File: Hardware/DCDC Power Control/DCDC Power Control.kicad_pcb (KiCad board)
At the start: 2 copper layers, 49 x 48 mm, 33 parts, among them J1 Conn_01x03, J2 Conn_01x02, J3 Conn_01x02, J4 Screw_Terminal_01x02, J5 Conn_01x01, Q2 SQJ479EP-T1_GE3, U1 CPC2025N

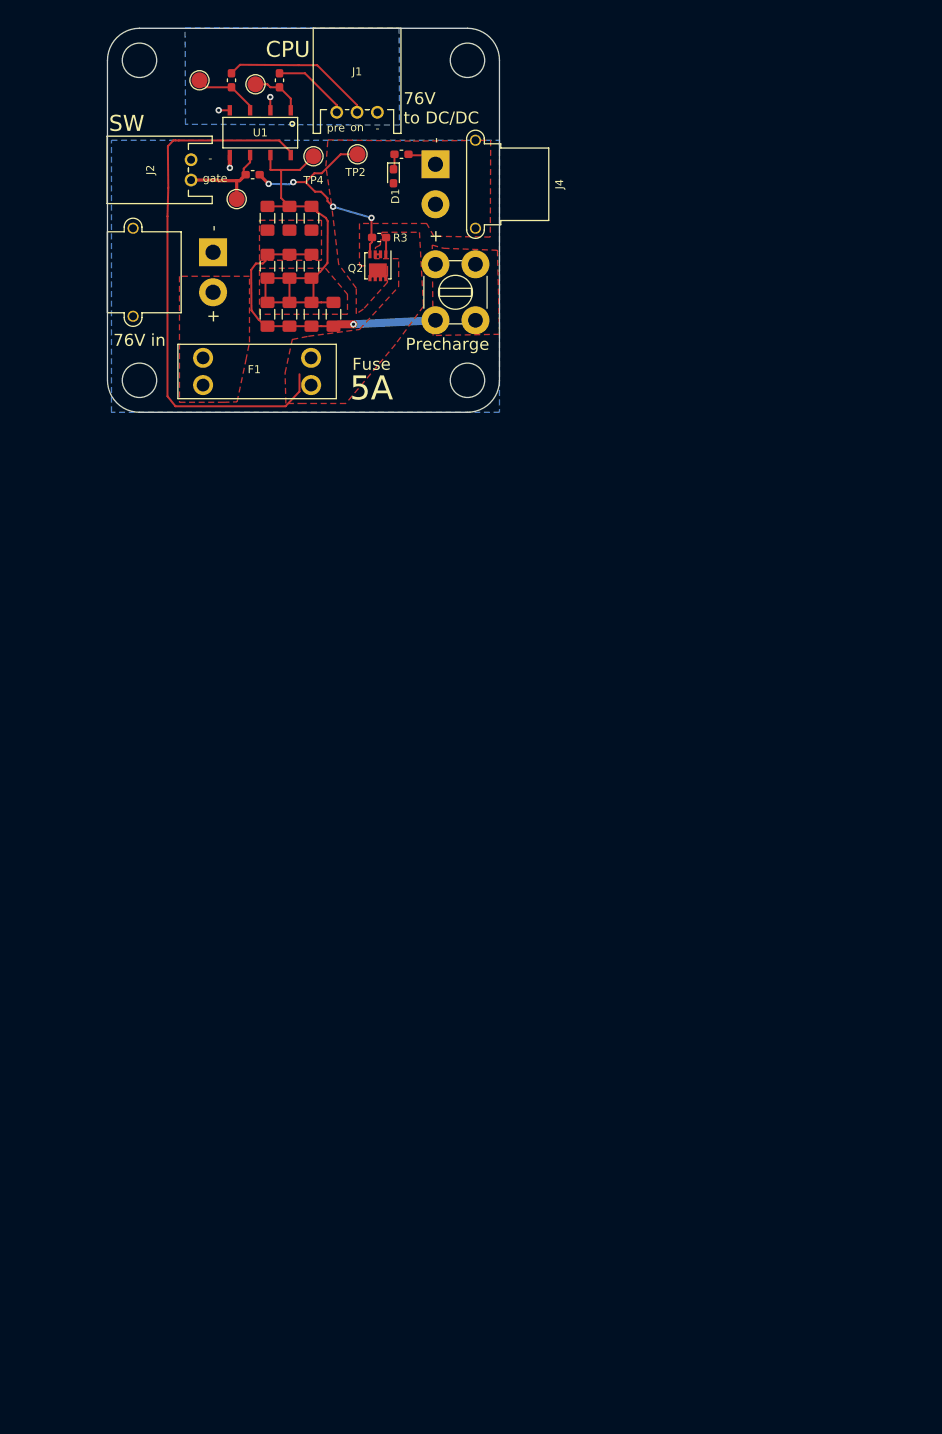
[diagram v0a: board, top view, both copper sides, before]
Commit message: Revision 2 of the DCDC Control PCB.
Now with precharge for both DC/DC and VESC, 150 ohm 45 W precharge resistors
(up to three per device).

Microcontroller to control the sequencing. ADC measurement of in vs out voltage
to determine when precharge is complete.
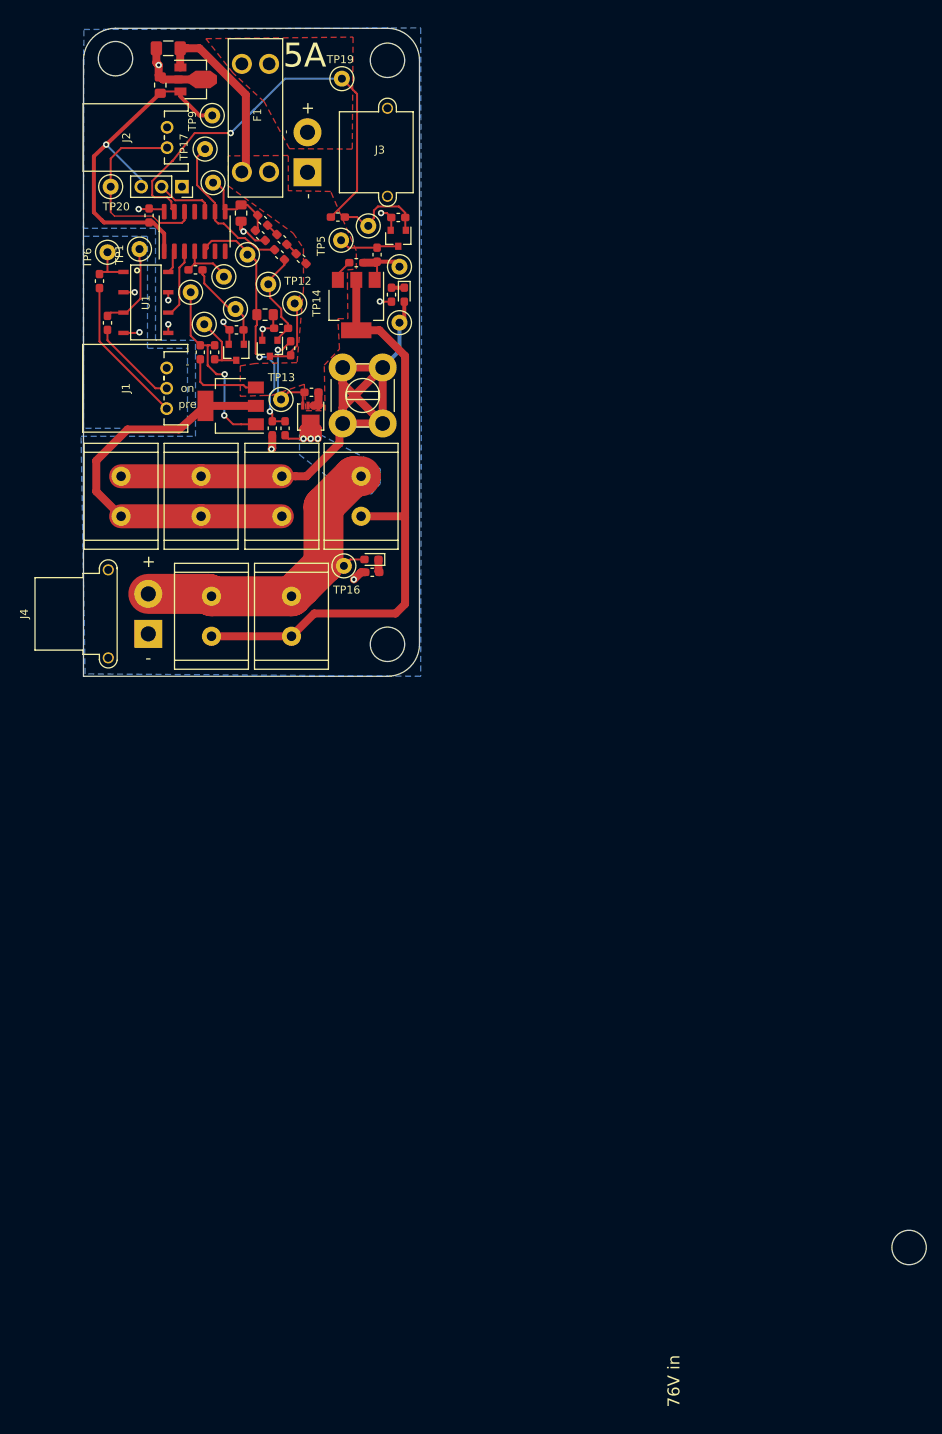
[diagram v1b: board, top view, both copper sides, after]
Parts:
- removed the H1 at (105.0, 46.0)
- removed H2: MountingHole, MountingHole:MountingHole_4.3mm_M4_ISO14580
- added C1: 100 nF/3.3V, Capacitor_SMD:C_0805_2012Metric_Pad1.15x1.40mm_HandSolder, F.Cu at (117.7, 65.1)
- added C2: 1 uF / 80V, Capacitor_SMD:C_1206_3216Metric_Pad1.42x1.75mm_HandSolder, F.Cu at (108.6, 44.5)
- added C3: 22 uF/3.3V, Capacitor_SMD:C_0805_2012Metric_Pad1.15x1.40mm_HandSolder, F.Cu at (107.6, 49.1)
- added C4: 100 nF/3.3V, Capacitor_SMD:C_0805_2012Metric_Pad1.15x1.40mm_HandSolder, F.Cu at (120.7, 77.8)
- added C5: 100 nF/3.3V, Capacitor_SMD:C_0603_1608Metric_Pad1.05x0.95mm_HandSolder, F.Cu at (106.2, 65.4)
- added D2: LED, LED_SMD:LED_0603_1608Metric_Pad1.05x0.95mm_HandSolder, F.Cu at (134.0, 108.4)
- added H1: MountingHole, MountingHole:MountingHole_4.3mm_M4_ISO14580, F.Cu at (102.0, 46.0)
- added H1: MountingHole, MountingHole:MountingHole_4.3mm_M4_ISO14580, F.Cu at (136.0, 46.0)
- added J6: Conn_01x03_Female, Connector_PinSocket_2.54mm:PinSocket_1x03_P2.54mm_Vertical, F.Cu at (110.3, 61.8)
- added Q1: BSS123, Package_TO_SOT_SMD:SOT-23, F.Cu at (117.1, 82.5)
- added Q3: BSS123, Package_TO_SOT_SMD:SOT-23, F.Cu at (137.3, 68.2)
- added Q4: MCT06P10, Package_TO_SOT_SMD:SOT-223-3_TabPin2, F.Cu at (132.1, 76.6)
- added Q5: BSS123, Package_TO_SOT_SMD:SOT-23, F.Cu at (121.3, 82.0)
- added Q6: SQJ479EP-T1_GE3, Package_SO:Vishay_PowerPAK_1212-8_Single, F.Cu at (126.4, 90.6)
- added R16: 15K, Resistor_SMD:R_0603_1608Metric_Pad1.05x0.95mm_HandSolder, F.Cu at (132.1, 71.3)
- added R17: 56k, Resistor_SMD:R_0603_1608Metric_Pad1.05x0.95mm_HandSolder, F.Cu at (134.7, 70.3)
- added R18: 150 Ohm, 45W, Resistor_THT:R_Radial_Power_L13.0mm_W9.0mm_P5.00mm, F.Cu at (124.0, 113.0)
- added R19: 10k, Resistor_SMD:R_0603_1608Metric_Pad1.05x0.95mm_HandSolder, F.Cu at (122.7, 79.5)
- added R20: 15K, Resistor_SMD:R_0603_1608Metric_Pad1.05x0.95mm_HandSolder, F.Cu at (126.5, 87.5)
- added R21: 56k, Resistor_SMD:R_0603_1608Metric_Pad1.05x0.95mm_HandSolder, F.Cu at (123.9, 82.0)
- added R22: 1k, Resistor_SMD:R_0603_1608Metric_Pad1.05x0.95mm_HandSolder, F.Cu at (112.0, 72.2)
- added R23: 1k, Resistor_SMD:R_0603_1608Metric_Pad1.05x0.95mm_HandSolder, F.Cu at (129.8, 65.6)
- added R24: 1k, Resistor_SMD:R_0603_1608Metric_Pad1.05x0.95mm_HandSolder, F.Cu at (122.5, 70.3)
- added R25: 150 Ohm, 45W, Resistor_THT:R_Radial_Power_L13.0mm_W9.0mm_P5.00mm, F.Cu at (102.7, 98.0)
- added R26: 150 Ohm, 45W, Resistor_THT:R_Radial_Power_L13.0mm_W9.0mm_P5.00mm, F.Cu at (122.8, 98.0)
- added R27: 150 Ohm, 45W, Resistor_THT:R_Radial_Power_L13.0mm_W9.0mm_P5.00mm, F.Cu at (132.7, 98.0)
- added R28: 150 Ohm, 45W, Resistor_THT:R_Radial_Power_L13.0mm_W9.0mm_P5.00mm, F.Cu at (114.0, 113.0)
- added TP10: TestPoint, TestPoint:TestPoint_Loop_D2.50mm_Drill1.0mm_LowProfile, F.Cu at (117.0, 77.1)
- added TP11: TestPoint, TestPoint:TestPoint_Loop_D2.50mm_Drill1.0mm_LowProfile, F.Cu at (133.6, 66.7)
- added TP12: TestPoint, TestPoint:TestPoint_Loop_D2.50mm_Drill1.0mm_LowProfile, F.Cu at (121.1, 74.0)
- added TP13: TestPoint, TestPoint:TestPoint_Loop_D2.50mm_Drill1.0mm_LowProfile, F.Cu at (122.7, 88.4)
- added TP14: TestPoint, TestPoint:TestPoint_Loop_D2.50mm_Drill1.0mm_LowProfile, F.Cu at (124.4, 76.4)
- added TP15: TestPoint, TestPoint:TestPoint_Loop_D2.50mm_Drill1.0mm_LowProfile, F.Cu at (137.5, 78.8)
- added TP16: TestPoint, TestPoint:TestPoint_Loop_D2.50mm_Drill1.0mm_LowProfile, F.Cu at (130.6, 109.2)
- added TP17: TestPoint, TestPoint:TestPoint_Loop_D2.50mm_Drill1.0mm_LowProfile, F.Cu at (113.2, 57.1)
- added TP18: TestPoint, TestPoint:TestPoint_Loop_D2.50mm_Drill1.0mm_LowProfile, F.Cu at (115.5, 73.0)
- added TP19: TestPoint, TestPoint:TestPoint_Loop_D2.50mm_Drill1.0mm_LowProfile, F.Cu at (130.3, 48.3)
- added TP20: TestPoint, TestPoint:TestPoint_Loop_D2.50mm_Drill1.0mm_LowProfile, F.Cu at (101.4, 61.8)
- added TP5: TestPoint, TestPoint:TestPoint_Loop_D2.50mm_Drill1.0mm_LowProfile, F.Cu at (130.2, 68.5)
- added TP7: TestPoint, TestPoint:TestPoint_Loop_D2.50mm_Drill1.0mm_LowProfile, F.Cu at (114.2, 61.3)
- added TP8: TestPoint, TestPoint:TestPoint_Loop_D2.50mm_Drill1.0mm_LowProfile, F.Cu at (118.5, 70.3)
- added TP9: TestPoint, TestPoint:TestPoint_Loop_D2.50mm_Drill1.0mm_LowProfile, F.Cu at (114.1, 52.9)
- added U2: NCP785AH33T1G, Package_TO_SOT_SMD:SOT-89-3, F.Cu at (111.6, 48.4)
- added U3: ATtiny414-SS, Package_SO:SOIC-14_3.9x8.7mm_P1.27mm, F.Cu at (111.9, 67.4)
- D1: value LED -> Or LED
- Q2: value SQJ479EP-T1_GE3 -> MCT06P10; footprint Package_SO:Vishay_PowerPAK_1212-8_Single -> Package_TO_SOT_SMD:SOT-223-3_TabPin2
- R10: value 11k/500mW -> 13.3k; footprint Resistor_SMD:R_1206_3216Metric_Pad1.42x1.75mm_HandSolder -> Resistor_SMD:R_0603_1608Metric_Pad1.05x0.95mm_HandSolder
- R11: value 11k/500mW -> 100k; footprint Resistor_SMD:R_1206_3216Metric_Pad1.42x1.75mm_HandSolder -> Resistor_SMD:R_0603_1608Metric_Pad1.05x0.95mm_HandSolder
- R12: value 11k/500mW -> 15K; footprint Resistor_SMD:R_1206_3216Metric_Pad1.42x1.75mm_HandSolder -> Resistor_SMD:R_0603_1608Metric_Pad1.05x0.95mm_HandSolder
- R13: value 11k/500mW -> 56k; footprint Resistor_SMD:R_1206_3216Metric_Pad1.42x1.75mm_HandSolder -> Resistor_SMD:R_0603_1608Metric_Pad1.05x0.95mm_HandSolder
- R14: value 11k/500mW -> 150 Ohm, 45W; footprint Resistor_SMD:R_1206_3216Metric_Pad1.42x1.75mm_HandSolder -> Resistor_THT:R_Radial_Power_L13.0mm_W9.0mm_P5.00mm
- R15: value 11k/500mW -> 10k; footprint Resistor_SMD:R_1206_3216Metric_Pad1.42x1.75mm_HandSolder -> Resistor_SMD:R_0603_1608Metric_Pad1.05x0.95mm_HandSolder
- R3: value 15K -> 47k 120 mW
- R4: value 56k -> 47k
- R5: value 10k -> 10M
- R6, R7: value 11k/500mW -> 10M; footprint Resistor_SMD:R_1206_3216Metric_Pad1.42x1.75mm_HandSolder -> Resistor_SMD:R_0603_1608Metric_Pad1.05x0.95mm_HandSolder
- R8: value 11k/500mW -> 1.33M; footprint Resistor_SMD:R_1206_3216Metric_Pad1.42x1.75mm_HandSolder -> Resistor_SMD:R_0603_1608Metric_Pad1.05x0.95mm_HandSolder
- R9: value 11k/500mW -> 300k; footprint Resistor_SMD:R_1206_3216Metric_Pad1.42x1.75mm_HandSolder -> Resistor_SMD:R_0603_1608Metric_Pad1.05x0.95mm_HandSolder
- TP1, TP2, TP3, TP4, TP6: footprint TestPoint:TestPoint_Pad_D2.0mm -> TestPoint:TestPoint_Loop_D2.50mm_Drill1.0mm_LowProfile
- moved H3 144.9 mm to (201.2, 194.4), turned to 90 degrees
- moved H4 73.7 mm to (136.0, 119.0), turned to 270 degrees
- moved J4 68.8 mm to (106.1, 117.7), turned to 90 degrees
- moved R4 51.9 mm to (134.1, 110.0)
- moved J1 41.9 mm to (108.4, 87.0), turned to 270 degrees
- moved R14 35.1 mm to (112.7, 98.0), turned to 270 degrees
- moved R1 34.1 mm to (101.0, 78.8), turned to 270 degrees
- moved R2 33.7 mm to (100.0, 73.6), turned to 270 degrees
- moved F1 31.7 mm to (119.5, 53.2), turned to 90 degrees
- moved TP6 28.0 mm to (101.0, 70.0), turned to 270 degrees
- moved TP2 27.1 mm to (111.4, 75.0), turned to 270 degrees
- moved U1 25.6 mm to (105.8, 76.3), turned to 270 degrees
- moved Q2 25.4 mm to (116.4, 89.2), turned to 180 degrees
- moved TP1 22.4 mm to (105.0, 69.6), turned to 270 degrees
- moved R9 20.3 mm to (123.2, 92.0), turned to 90 degrees
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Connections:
- net /ON renamed /DCDC_ON_IN
- net /PRECHARGE_ON renamed /VESC_PRECHARGE_IN
- D1 pad 2: Net-(D1-Pad2) -> /VESC_OUT
- J2 pad 2: /POWER_GATE -> /SWITCH_B
- J4 pad 2: Net-(D1-Pad2) -> /DCDC_OUT
- J5 pad 1: /PRECHARGE_POST_R -> /VESC_OUT
- Q2 pad 1: +BATT -> /Power Switches/Q2_GATE
- Q2 pad 2: +BATT -> /Power Switches/VESC_PRE_PRECHARGE
- R10 pad 1: /PRECHARGE_POST_R -> /Microcontroller/DCDC_ADC
- R10 pad 2: /PRECHARGE_PRE_R -> GNDPWR
- R11 pad 1: /PRECHARGE_POST_R -> Net-(Q1-Pad1)
- R11 pad 2: /PRECHARGE_PRE_R -> GNDPWR
- R12 pad 1: /PRECHARGE_POST_R -> +BATT
- R12 pad 2: /PRECHARGE_PRE_R -> /Power Switches/Q2_GATE
- R13 pad 1: /PRECHARGE_POST_R -> /Power Switches/Q2_GATE
- R13 pad 2: /PRECHARGE_PRE_R -> Net-(Q1-Pad3)
- R14 pad 1: /PRECHARGE_POST_R -> /VESC_OUT
- R14 pad 2: /PRECHARGE_PRE_R -> /Power Switches/VESC_PRE_PRECHARGE
- R15 pad 1: /PRECHARGE_POST_R -> Net-(Q3-Pad1)
- R15 pad 2: /PRECHARGE_PRE_R -> GNDPWR
- R3 pad 1: +BATT -> Net-(D1-Pad1)
- R3 pad 2: /Q2_GATE -> GNDPWR
- R4 pad 1: /Q2_GATE -> Net-(D2-Pad1)
- R4 pad 2: /POWER_GATE -> GNDPWR
- R5 pad 1: Net-(D1-Pad1) -> +BATT
- R5 pad 2: GNDPWR -> Net-(R5-Pad2)
- R6 pad 1: /PRECHARGE_POST_R -> Net-(R5-Pad2)
- R6 pad 2: /PRECHARGE_PRE_R -> Net-(R6-Pad2)
- R7 pad 1: /PRECHARGE_POST_R -> Net-(R6-Pad2)
- R7 pad 2: /PRECHARGE_PRE_R -> /Microcontroller/VBATT_ADC
- R8 pad 1: /PRECHARGE_POST_R -> /Microcontroller/VBATT_ADC
- R8 pad 2: /PRECHARGE_PRE_R -> GNDPWR
- R9 pad 1: /PRECHARGE_POST_R -> /DCDC_OUT
- R9 pad 2: /PRECHARGE_PRE_R -> /Microcontroller/DCDC_ADC
- TP2 pad 1: /Q2_GATE -> /Power Switches/Q2_GATE
- TP3 pad 1: /POWER_GATE -> Net-(Q1-Pad3)
- TP4 pad 1: /PRECHARGE_PRE_R -> /Power Switches/Q4_GATE
- U1 pad 6: /POWER_GATE -> /DCDC_ON
- U1 pad 7: /PRECHARGE_PRE_R -> GNDPWR
- U1 pad 8: +BATT -> /VESC_PRECHARGE
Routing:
- net /VESC_OUT: track 0.00 -> 83.0 mm
- net /Power Switches/DCDC_PRE_PRECHARGE: track 0.00 -> 76.2 mm
- net /Microcontroller/DCDC_PRECHARGE_GATE: track 0.00 -> 55.6 mm, vias 0 -> 1
- net /PRECHARGE_PRE_R: track 53.7 -> 0.00 mm
- net /DCDC_OUT: track 0.00 -> 52.4 mm, vias 0 -> 3
- net /Power Switches/VESC_PRE_PRECHARGE: track 0.00 -> 51.0 mm
- net +3V3: track 0.00 -> 45.9 mm, vias 0 -> 1
- net /PRECHARGE_POST_R: track 38.2 -> 0.00 mm, vias 1 -> 0
- net /Microcontroller/DCDC_ADC: track 0.00 -> 33.3 mm, vias 0 -> 2
- net +BATT: track 70.7 -> 38.3 mm
- net GNDPWR: track 6.47 -> 36.0 mm, vias 1 -> 11
- net /Q2_GATE: track 29.3 -> 0.00 mm, vias 4 -> 0
- net /SWITCH_B: track 0.00 -> 24.8 mm
- net /Power Switches/Q2_GATE: track 0.00 -> 23.6 mm, vias 0 -> 2
- net /Microcontroller/DCDC_GATE: track 0.00 -> 19.1 mm
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- added copper zone on B.Cu, net /DCDC_OUT
- removed copper zone on F.Cu, net /PRECHARGE_POST_R
- removed copper zone on F.Cu, net /PRECHARGE_PRE_R
- removed copper zone on F.Cu, net Net-(D1-Pad2)
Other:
- board size 49 x 48 mm -> 42 x 81 mm
- net class 72V/1.5A added: clearance 0.3, trace_width 1, via_dia 0.8, via_drill 0.4
- net class 72V/5A: trace_width 1 -> 5
- rule trace_min: 0.2 -> 0.1524
- board text added: "DC/DC & Precharge rev 2"
- board text removed: "76V to DC/DC"
- board text removed: "DC/DC Power Switch & Precharge version 1"
- board text removed: "Fuse"
- board text removed: "Precharge"
- board text removed: "gate"

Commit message: Older PCB updates
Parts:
- removed the H1 at (136.0, 46.0)
- added D3: LED, LED_SMD:LED_0603_1608Metric_Castellated, F.Cu at (118.1, 72.0)
- added J7: Conn_01x02, Connector_PinHeader_2.54mm:PinHeader_1x02_P2.54mm_Vertical, F.Cu at (119.4, 69.6)
- added R29: ?, Resistor_SMD:R_0603_1608Metric_Pad1.05x0.95mm_HandSolder, F.Cu at (120.1, 74.9)
- added TP21: TestPoint, TestPoint:TestPoint_Loop_D2.50mm_Drill1.0mm_LowProfile, F.Cu at (101.0, 70.1)
- added TP22: TestPoint, TestPoint:TestPoint_Loop_D2.50mm_Drill1.0mm_LowProfile, F.Cu at (140.8, 111.5)
- C1, C4: footprint Capacitor_SMD:C_0805_2012Metric_Pad1.15x1.40mm_HandSolder -> Capacitor_SMD:C_0603_1608Metric_Pad1.05x0.95mm_HandSolder
- J6: value Conn_01x03_Female -> Conn_01x04_Female; footprint Connector_PinSocket_2.54mm:PinSocket_1x03_P2.54mm_Vertical -> Connector_PinSocket_2.54mm:PinSocket_1x04_P2.54mm_Vertical
- Q6: footprint Package_SO:Vishay_PowerPAK_1212-8_Single -> erland-footprints:Q-VISHAY-PowerPAK SO-8L Single
- moved H3 160.5 mm to (140.0, 46.0), turned to 0 degrees
- moved TP20 13.3 mm to (106.4, 49.5)
- moved R20 8.11 mm to (126.1, 79.4)
- moved TP8 6.73 mm to (123.5, 74.8)
- moved TP16 6.29 mm to (134.5, 114.1)
- moved TP12 6.04 mm to (126.5, 71.3)
- moved TP19 4.96 mm to (134.0, 45.0)
- moved J3 4.80 mm to (130.8, 60.0)
- moved R27 4.54 mm to (132.1, 102.5), turned to 0 degrees
- moved D1 4.00 mm to (142.1, 75.3)
- moved H4 4.00 mm to (140.0, 119.0)
- moved Q3 4.00 mm to (141.3, 68.2)
- moved Q4 4.00 mm to (136.1, 76.6)
- moved R15 4.00 mm to (141.3, 65.7)
- moved R16 4.00 mm to (136.1, 71.3)
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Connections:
- J6 pad 1: GNDPWR -> /Microcontroller/UDPI
- J6 pad 2: /Microcontroller/UDPI -> GNDPWR
- U3 pad 11: (no net) -> /Microcontroller/DCDC_PRECHARGE_GATE
- U3 pad 13: /Microcontroller/DCDC_PRECHARGE_GATE -> /Microcontroller/PA3
- U3 pad 6: (no net) -> /Microcontroller/PB3
- U3 pad 7: (no net) -> /Microcontroller/PB2
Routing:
- net /VESC_OUT: track 83.0 -> 29.9 mm
- net +BATT: track 38.3 -> 23.0 mm
- net /Microcontroller/DCDC_PRECHARGE_GATE: track 55.6 -> 66.7 mm
- net /DCDC_OUT: track 52.4 -> 43.5 mm, vias 3 -> 9
- net /Microcontroller/PB3: track 0.00 -> 7.46 mm
- net /Microcontroller/PA3: track 0.00 -> 6.78 mm
- net /Power Switches/DCDC_PRE_PRECHARGE: track 76.2 -> 69.8 mm
- net +3V3: track 45.9 -> 40.2 mm
- net Net-(R2-Pad1): track 5.59 -> 10.4 mm
- net /Microcontroller/UDPI: track 7.33 -> 3.20 mm
- net /Microcontroller/DCDC_ADC: track 33.3 -> 37.3 mm
- net GNDPWR: track 36.0 -> 39.7 mm, vias 11 -> 12
- net /Microcontroller/PB2: track 0.00 -> 3.55 mm
- net Net-(Q5-Pad1): track 12.3 -> 14.9 mm
- net /SWITCH_B: track 24.8 -> 27.2 mm
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- added copper zone on F.Cu, net /DCDC_OUT
- added copper zone on F.Cu, net /VESC_OUT
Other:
- board size 42 x 81 mm -> 46 x 81 mm
- board text added: "Battery"
- board text added: "DC/DC"
- board text added: "To DC/DC"
- board text added: "To VESC"
- board text added: "VESC"
- board text added: "d"
- board text added: "g"
- board text added: "s"
